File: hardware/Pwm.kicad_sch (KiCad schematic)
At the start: 69 parts, among them J10 Conn_01x03_Male, J11 Conn_01x03_Male, J12 Conn_01x03_Male, J13 Conn_01x03_Male, J14 Conn_01x03_Male, J15 Conn_01x03_Male, J16 JST XH, J17 KF350, J18 JST XH, J19 JST XH, J20 KF350, J21 JST XH, J4 JST XH, J5 KF129, J6 KF350, J7 Conn_01x03_Male, J8 Conn_01x03_Male, J9 Conn_01x03_Male, U6 74HCT04

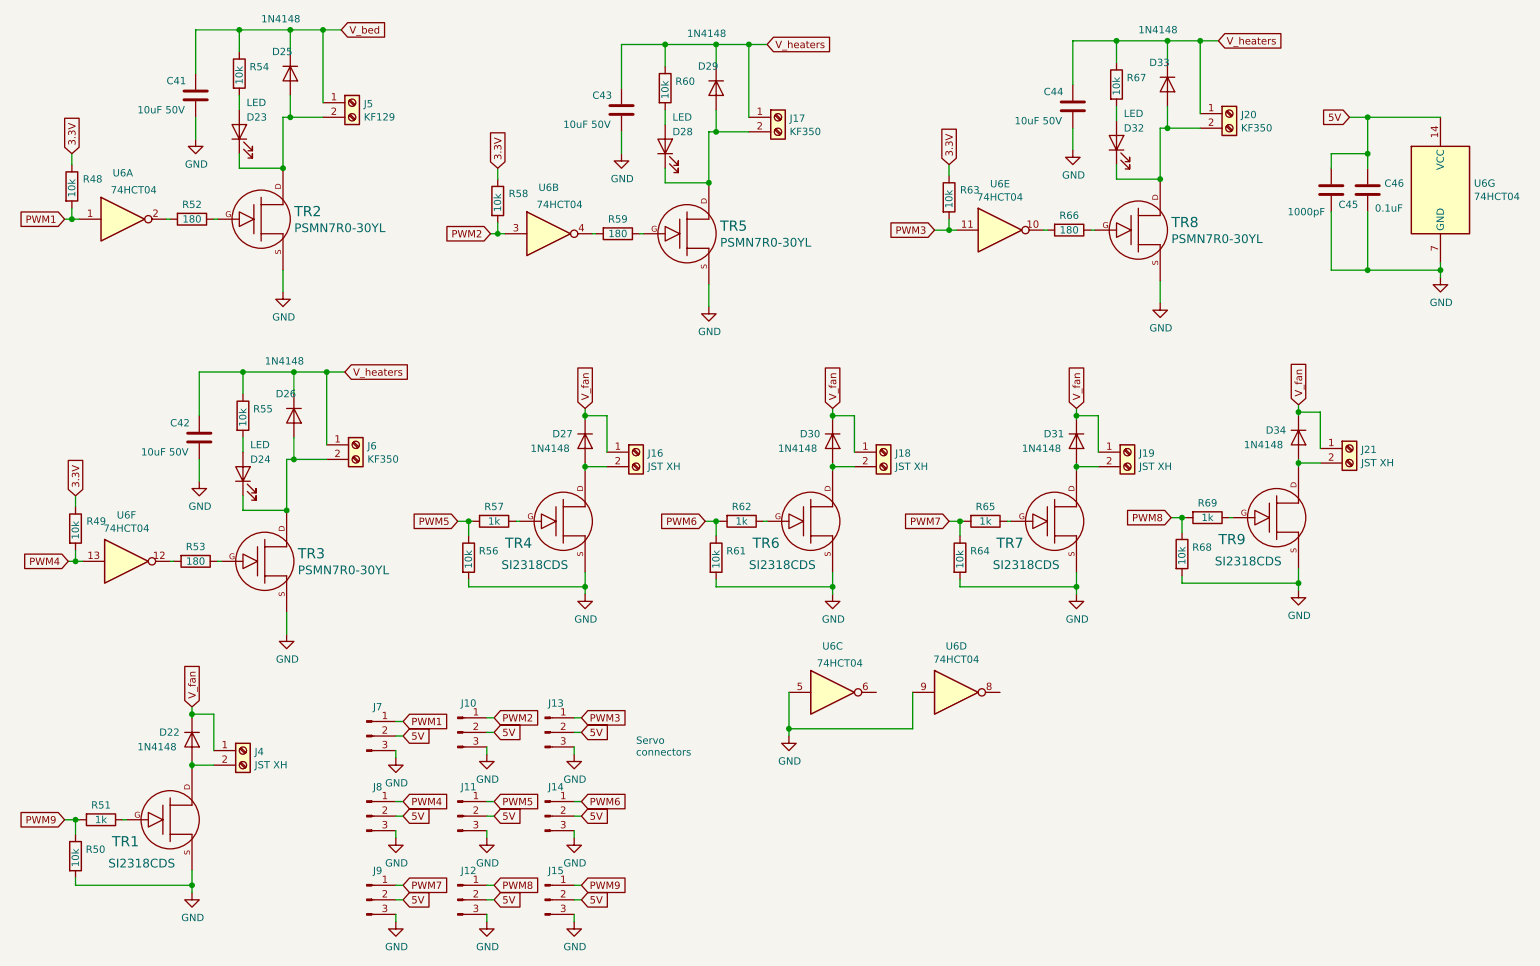
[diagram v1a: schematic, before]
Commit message: Update the 1N4148 diodes to B5819W. The 1N was too puny to serve as protection.
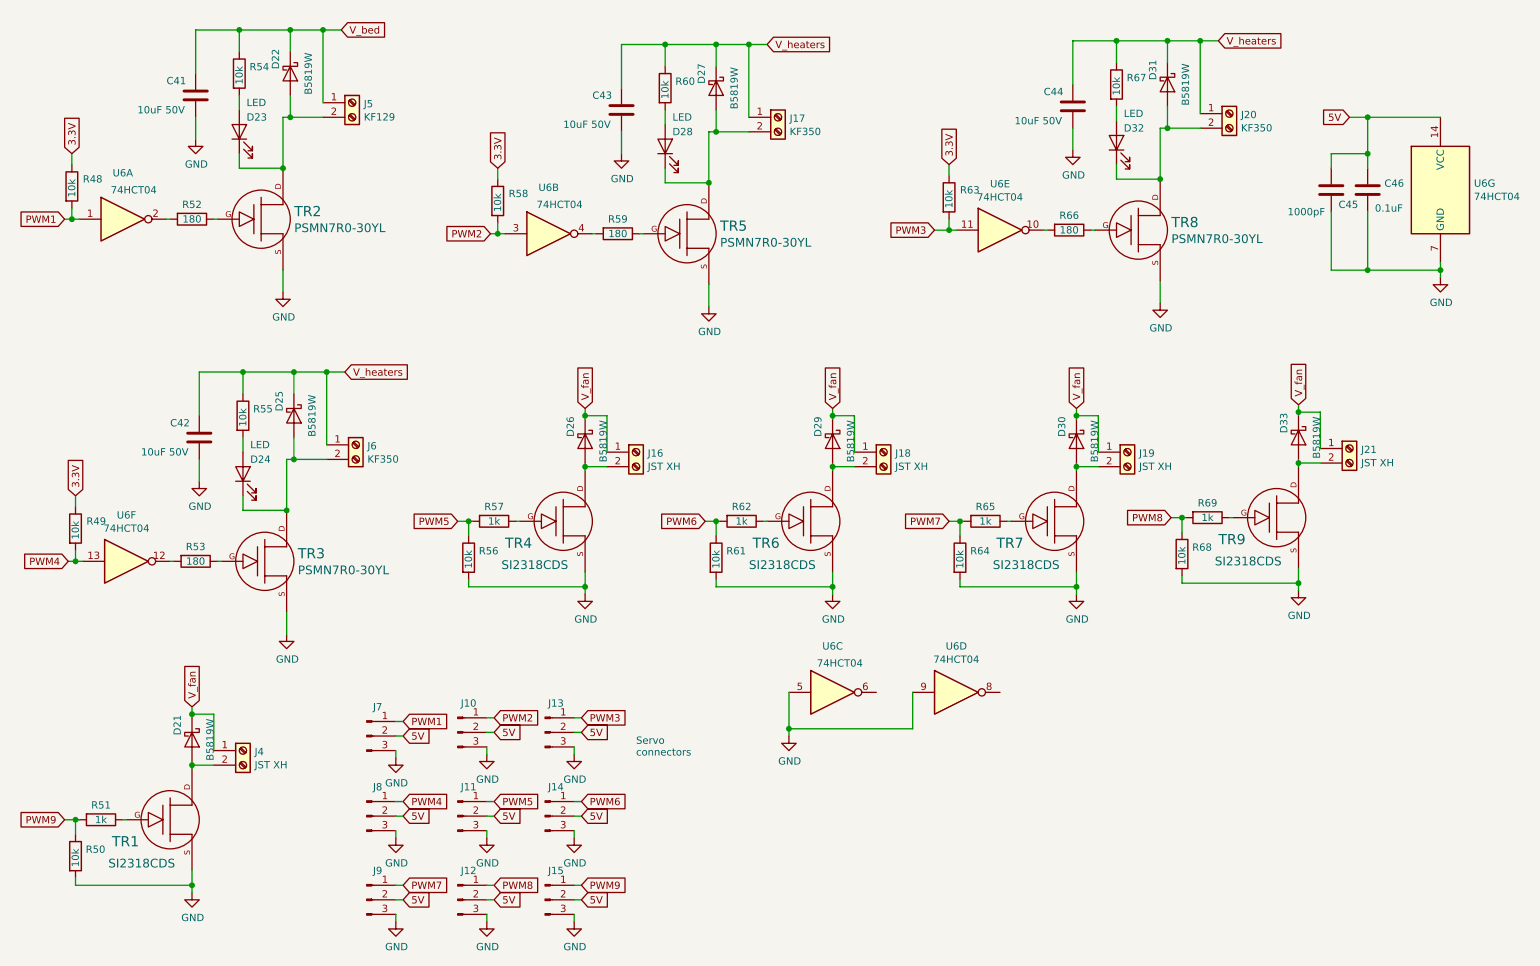
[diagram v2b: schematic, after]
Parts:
- removed D22, D25, D26, D27, D29, D30, D31, D33, D34: 1N4148, Diode_SMD:D_SOD-323_HandSoldering, symbol Device:D
- added D21, D22, D25, D26, D27, D29, D30, D31, D33: B5819W, Diode_SMD:D_SOD-123, symbol Device:D_Schottky
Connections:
- net V_bed: now also D22.1 (K)
- net V_fan: now also D21.1 (K), D26.1 (K), D29.1 (K), D30.1 (K), D33.1 (K)
- net V_heaters: now also D25.1 (K), D27.1 (K), D31.1 (K)
- net at D23.1 (K), J5.2 (Pin_2), TR2.D: now also D22.2 (A)
- net at D28.1 (K), J17.2 (Pin_2), TR5.D: now also D27.2 (A)
- net at D32.1 (K), J20.2 (Pin_2), TR8.D: now also D31.2 (A)
- net at D24.1 (K), J6.2 (Pin_2), TR3.D: now also D25.2 (A)
- net at J16.2 (Pin_2), TR4.D: now also D26.2 (A)
- net at J18.2 (Pin_2), TR6.D: now also D29.2 (A)
- net at J19.2 (Pin_2), TR7.D: now also D30.2 (A)
- net at J21.2 (Pin_2), TR9.D: now also D33.2 (A)
- net at J4.2 (Pin_2), TR1.D: now also D21.2 (A)
